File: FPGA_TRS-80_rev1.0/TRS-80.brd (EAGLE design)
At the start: 160 x 100 mm, 165 parts, among them IC2 CP2102, U1 EP4CE6E22C8N, X1 PN61729-S

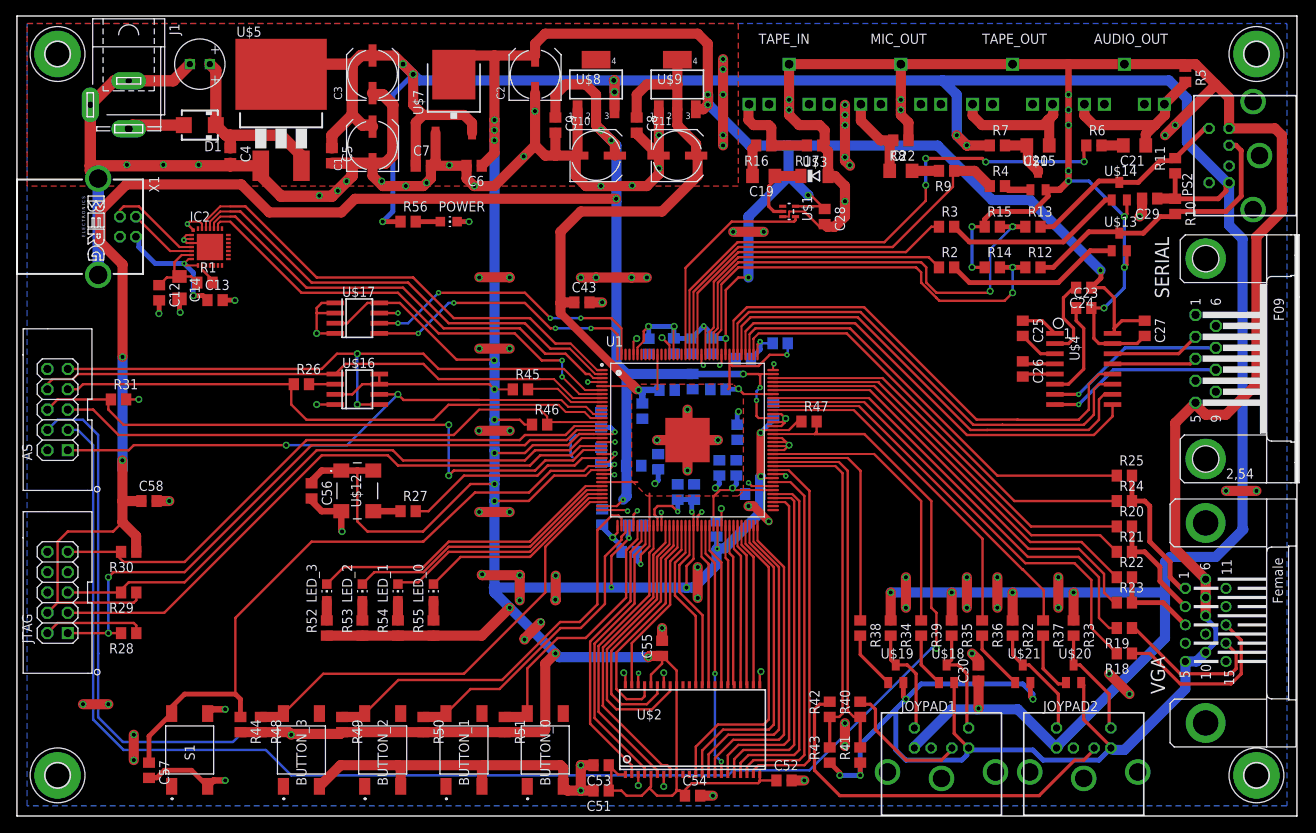
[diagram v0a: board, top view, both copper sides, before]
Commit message: fixed HDMI signal names in V2.0, fixed missing I2C resistors in V1.0
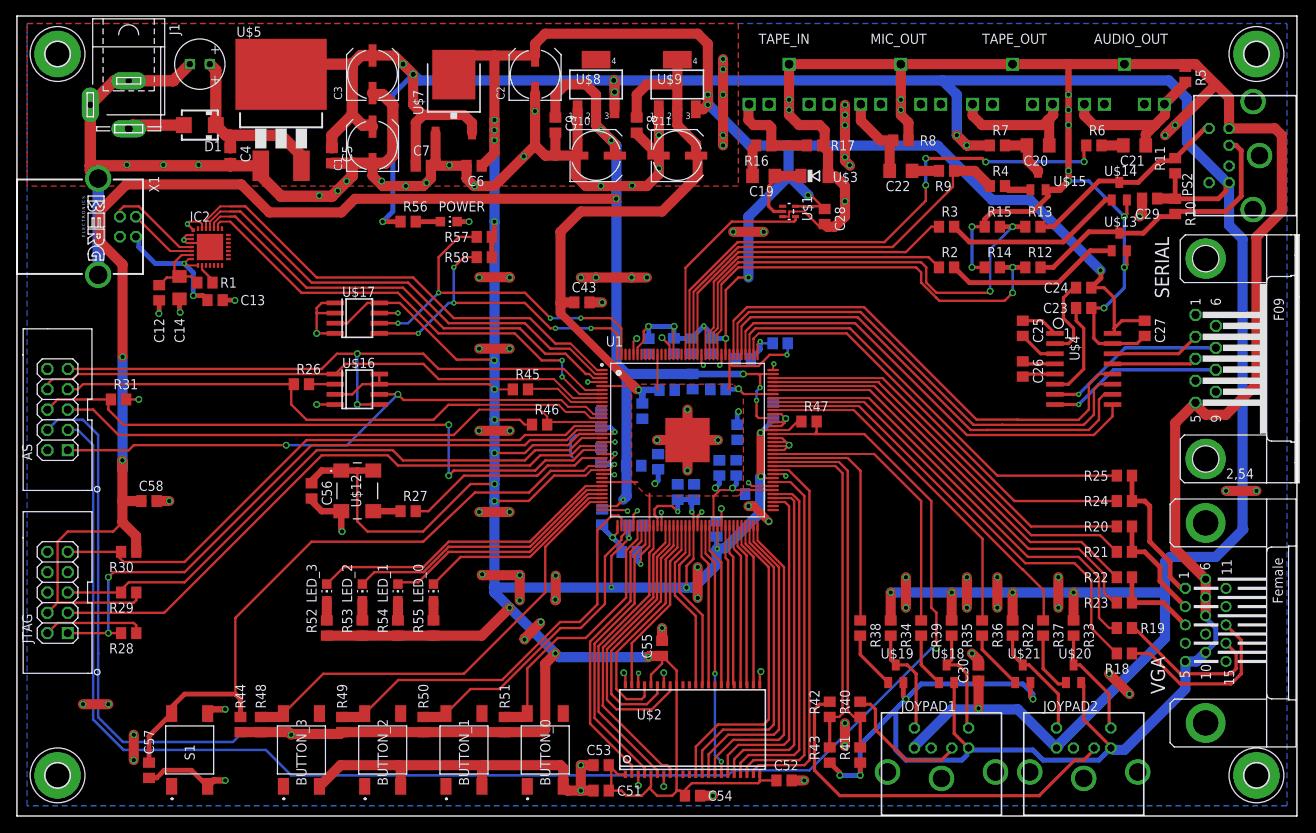
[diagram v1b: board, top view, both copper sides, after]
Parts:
- added R57, R58: 5K6, rcl:R0805
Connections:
- net 3V3: now also R57.1, R58.1
- net I2C_SCL: now also R57.2
- net I2C_SDA: now also R58.2
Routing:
- net I2C_SCL: track 37.0 -> 47.2 mm
- net I2C_SDA: track 35.5 -> 43.3 mm, vias 4 -> 5
- net 3V3: track 704.7 -> 709.5 mm, vias 32 -> 33
